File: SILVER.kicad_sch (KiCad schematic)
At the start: 51 parts, among them J1 Conn_01x13, J10 Conn_02x22_Odd_Even_MountingP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, J3 MPU6050, J4 MotorL, J5 MotorR, J6 XT60-M, J7 STLINK, J8 Conn_01x04_Pin, J9 Conn_02x22_Odd_Even_MountingP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, Q1 FCD600N60Z, Q2 FCD600N60Z, SW1 SW_DIP_x01, U1 VNH5019A-E, U2 VNH5019A-E, U4 LM2596S-5.0

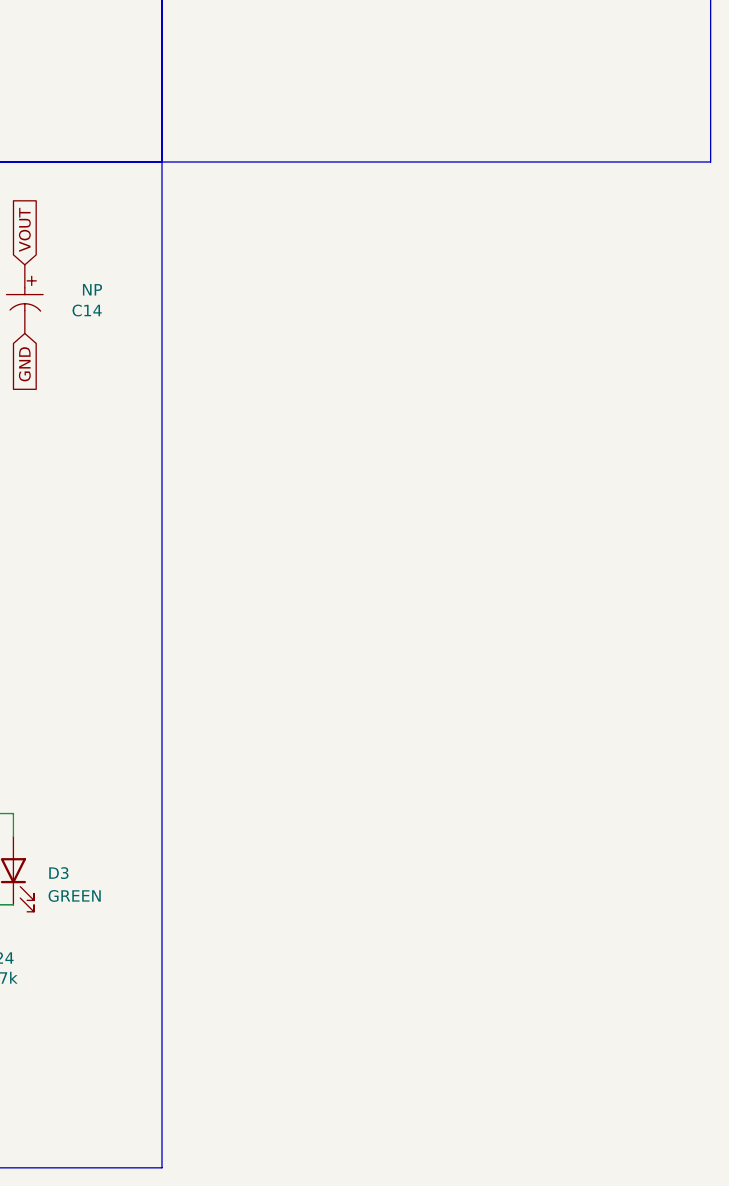
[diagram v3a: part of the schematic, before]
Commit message: Added ultrasonic sensor placement
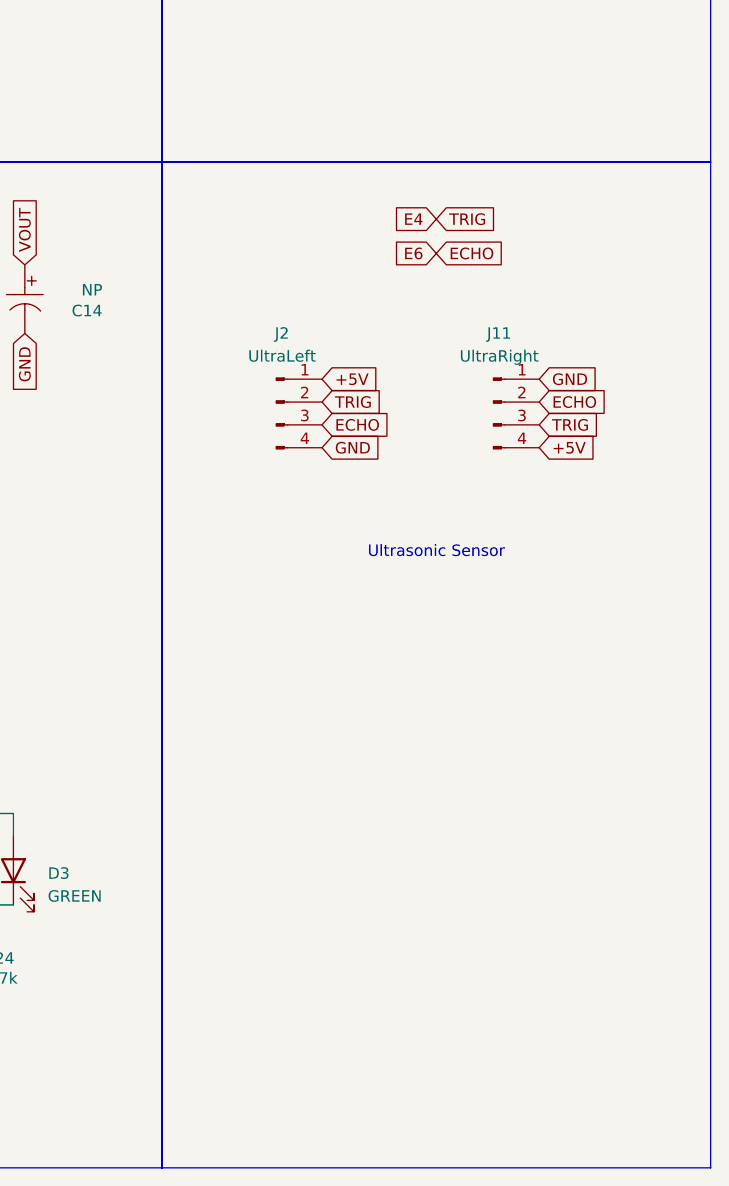
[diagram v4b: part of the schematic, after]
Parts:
- added J11: UltraRight, Connector_PinSocket_2.54mm:PinSocket_1x04_P2.54mm_Vertical, symbol Connector:Conn_01x04_Pin
- added J2: UltraLeft, Connector_PinSocket_2.54mm:PinSocket_1x04_P2.54mm_Vertical, symbol Connector:Conn_01x04_Pin
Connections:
- net +5V: now also J11.4 (Pin_4), J2.1 (Pin_1)
- net E4: now also J11.3 (Pin_3), J2.2 (Pin_2)
- net E6: now also J11.2 (Pin_2), J2.3 (Pin_3)
- net GND: now also J11.1 (Pin_1), J2.4 (Pin_4)
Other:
- note added: "Ultrasonic Sensor"

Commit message: pcbv1.0
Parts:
- removed C1, C5: 33nF, Capacitor_SMD:C_0805_2012Metric, symbol VNH5019-altium-import:root_3_33nF_
- removed C12, C15, C2, C4, C6, C8: 0.1u, Capacitor_SMD:C_0805_2012Metric, symbol VNH5019-altium-import:root_0_0.1u_
- removed C13, C14, C16, C17: NP, Capacitor_SMD:C_Elec_6.3x5.4, symbol VNH5019-altium-import:root_0_47uF_
- removed C18, C19: 330u, Capacitor_SMD:CP_Elec_8x10.5, symbol LM2596-altium-import:root_0_330u_
- removed C3, C7: 47uF, Capacitor_SMD:C_Elec_6.3x5.4, symbol VNH5019-altium-import:root_0_47uF_
- removed D3, D6: GREEN, LED_SMD:LED_0603_1608Metric, symbol Device:LED
- removed D4, D5: RED, LED_SMD:LED_0603_1608Metric, symbol Device:LED
- removed D7: SS34, Diode_SMD:D_SMA, symbol LM2596-altium-import:root_1_SS34_
- removed L2: 47uH, Inductor_SMD:L_12x12mm_H6mm, symbol LM2596-altium-import:root_0_47uH_
- removed Q1, Q2: FCD600N60Z, Package_TO_SOT_SMD:TO-252-2, symbol VNH5019-altium-import:root_1_FCD600N60Z_
- removed R1, R10: 10k, Resistor_SMD:R_0508_1220Metric, symbol VNH5019-altium-import:root_1_10k_
- removed R11, R12, R15, R2, R3, R6: 1k, Resistor_SMD:R_0508_1220Metric, symbol VNH5019-altium-import:root_0_1k_
- removed R16, R7: 1k, Resistor_SMD:R_0508_1220Metric, symbol VNH5019-altium-import:root_1_1k_
- removed R18, R9: 10k, Resistor_SMD:R_0508_1220Metric, symbol VNH5019-altium-import:root_0_10k_
- removed R24, R25: 4.7k, Resistor_SMD:R_0508_1220Metric, symbol VNH5019-altium-import:root_1_4.7k_
- removed U1, U2: VNH5019A-E, Package_SO:ST_MultiPowerSO-30, symbol VNH5019-altium-import:root_0_VNH5019A-E_
- removed U4: LM2596S-5.0, Package_TO_SOT_SMD:TO-263-5_TabPin3, symbol LM2596-altium-import:root_0_LM2596S-5.0_
- added D1: LED_RGBK, Connector_PinSocket_2.54mm:PinSocket_2x02_P2.54mm_Vertical, symbol Device:LED_RGBK
- added J12, J18: Conn_01x02_Pin, Connector_PinHeader_2.54mm:PinHeader_1x02_P2.54mm_Vertical, symbol Connector:Conn_01x02_Pin
- added J14, J15, J16, J17: Screw_Terminal_01x02, TerminalBlock:TerminalBlock_MaiXu_MX126-5.0-02P_1x02_P5.00mm, symbol Connector:Screw_Terminal_01x02
- J1: footprint Connector_FFC-FPC:Hirose_FH12-13S-0.5SH_1x13-1MP_P0.50mm_Horizontal -> Connector_PinHeader_2.54mm:PinHeader_1x13_P2.54mm_Vertical
- J7: now left out of the parts list
- SW1: footprint Library:SW_RB141C1100 -> Library:KCD11-101
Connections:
- net +12V: now also J14.1 (Pin_1)
- net +5V: now also J17.1 (Pin_1)
- net B8: now also J11.2 (Pin_2)
- net D12: now also J18.1 (Pin_1)
- net D13: now also J18.2 (Pin_2)
- net D14: now also J12.1 (Pin_1)
- net D15: now also J12.2 (Pin_2)
- net E6: no longer J11.2 (Pin_2)
- net E7: now also D1.1 (RA)
- net E8: now also D1.2 (GA)
- net E9: now also D1.3 (BA)
- net GND: now also D1.4 (K), J14.2 (Pin_2), J17.2 (Pin_2)
- net OUTA_L: now also J16.1 (Pin_1)
- net OUTA_R: now also J15.1 (Pin_1)
- net OUTB_L: now also J16.2 (Pin_2)
- net OUTB_R: now also J15.2 (Pin_2)
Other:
- note added: "Sensors connector"
- note removed: "35V"
- note removed: "Sensors ribbon flex connector"
- moved on the sheet: J1, J11, J2

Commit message: SILVER PCB v2.0
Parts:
- removed D1: LED_RGBK, Connector_PinSocket_2.54mm:PinSocket_2x02_P2.54mm_Vertical, symbol Device:LED_RGBK
- added D2: APFA3010, Connector_PinSocket_2.54mm:PinSocket_2x02_P2.54mm_Vertical, symbol LED:APFA3010
- added R1: R, Resistor_THT:R_Axial_DIN0204_L3.6mm_D1.6mm_P2.54mm_Vertical, symbol Device:R
- J1: footprint Connector_PinHeader_2.54mm:PinHeader_1x13_P2.54mm_Vertical -> Connector_PinHeader_2.54mm:PinHeader_1x13_P2.54mm_Vertical_SMD_Pin1Left
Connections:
- net +5V: now also R1.1
- net E7: now also D2.1 (R)
- net E8: now also D2.3 (G)
- net E9: now also D2.4 (B)
- new net: D2.2 (A), R1.2
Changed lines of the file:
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@@
 		)
 	)
-	(global_label "GND"
-		(shape input)
-		(at 209.55 214.63 180)
-		(fields_autoplaced yes)
-		(effects
-			(font
-				(size 1.27 1.27)
-			)
-			(justify right)
-		)
-		(property "Intersheetrefs" "${INTERSHEET_REFS}"
-			(at 202.6943 214.63 0)
-			(effects
-				(font
-					(size 1.27 1.27)
-				)
-				(justify right)
-				(hide yes)
-			)
-		)
-	)
 	(global_label "INT"
 		(shape input)
@@
 		)
 	)
+	(global_label "+5V"
+		(shape input)
+		(at 201.93 214.63 180)
+		(fields_autoplaced yes)
+		(effects
+			(font
+				(size 1.27 1.27)
+			)
+			(justify right)
+		)
+		(property "Intersheetrefs" "${INTERSHEET_REFS}"
+			(at 195.0743 214.63 0)
+			(effects
+				(font
+					(size 1.27 1.27)
+				)
+				(justify right)
+				(hide yes)
+			)
+		)
+	)
 	(global_label "E3"
 		(shape input)
@@
 	)
 	(symbol
+		(lib_id "Device:R")
+		(at 205.74 214.63 90)
+		(unit 1)
+		(exclude_from_sim no)
+		(in_bom yes)
+		(on_board yes)
+		(dnp no)
+		(fields_autoplaced yes)
+		(property "Reference" "R1"
+			(at 205.74 208.28 90)
+			(effects
+				(font
+					(size 1.27 1.27)
+				)
+			)
+		)
+		(property "Value" "R"
+			(at 205.74 210.82 90)
+			(effects
+				(font
+					(size 1.27 1.27)
+				)
+			)
+		)
+		(property "Footprint" "Resistor_THT:R_Axial_DIN0204_L3.6mm_D1.6mm_P2.54mm_Vertical"
+			(at 205.74 216.408 90)
+			(effects
+				(font
+					(size 1.27 1.27)
+				)
+				(hide yes)
+			)
+		)
+		(property "Datasheet" "~"
+			(at 205.74 214.63 0)
+			(effects
+				(font
+					(size 1.27 1.27)
+				)
+				(hide yes)
+			)
+		)
+		(property "Description" "Resistor"
+			(at 205.74 214.63 0)
+			(effects
+				(font
+					(size 1.27 1.27)
+				)
+				(hide yes)
+			)
+		)
+		(pin "1"
+		)
+		(pin "2"
+		)
+		(instances
+			(project ""
+				(path "/ac1a16b8-a2a7-4153-a4fd-a818d49ce2b8"
+					(reference "R1")
+					(unit 1)
+				)
+			)
+		)
+	)
+	(symbol
 		(lib_id "STLINK-altium-import:root_0_NUCLEO-F401-STLINKEXTRACT_")
 		(at 66.04 52.07 0)
@@
 			)
 		)
-		(property "Footprint" "Connector_PinHeader_2.54mm:PinHeader_1x13_P2.54mm_Vertical"
+		(property "Footprint" "Connector_PinHeader_2.54mm:PinHeader_1x13_P2.54mm_Vertical_SMD_Pin1Left"
 			(at 191.77 66.04 0)
 			(effects
@@
 	)
 	(symbol
-		(lib_id "Device:LED_RGBK")
-		(at 214.63 214.63 0)
-		(unit 1)
-		(exclude_from_sim no)
-		(in_bom yes)
-		(on_board yes)
-		(dnp no)
-		(fields_autoplaced yes)
-		(property "Reference" "D1"
-			(at 214.63 200.66 0)
-			(effects
-				(font
-					(size 1.27 1.27)
-				)
-			)
-		)
-		(property "Value" "LED_RGBK"
-			(at 214.63 203.2 0)
-			(effects
-				(font
-					(size 1.27 1.27)
-				)
-			)
-		)
-		(property "Footprint" "Connector_PinSocket_2.54mm:PinSocket_2x02_P2.54mm_Vertical"
-			(at 214.63 215.9 0)
-			(effects
-				(font
-					(size 1.27 1.27)
-				)
-				(hide yes)
-			)
-		)
-		(property "Datasheet" "~"
-			(at 214.63 215.9 0)
-			(effects
-				(font
-					(size 1.27 1.27)
-				)
-				(hide yes)
-			)
-		)
-		(property "Description" "RGB LED, red/green/blue/cathode"
-			(at 214.63 214.63 0)
-			(effects
-				(font
-					(size 1.27 1.27)
-				)
-				(hide yes)
-			)
-		)
-		(pin "2"
-		)
-		(pin "1"
-		)
-		(pin "4"
-		)
-		(pin "3"
-		)
-		(instances
-			(project ""
-				(path "/ac1a16b8-a2a7-4153-a4fd-a818d49ce2b8"
-					(reference "D1")
-					(unit 1)
-				)
-			)
-		)
-	)
-	(symbol
 		(lib_id "Switch:SW_DIP_x01")
 		(at 60.96 99.06 0)
@@
 					(unit 1)
 				)
+			)
+		)
+	)
+	(symbol
+		(lib_id "LED:APFA3010")
+		(at 214.63 214.63 0)
+		(mirror y)
+		(unit 1)
+		(exclude_from_sim no)
+		(in_bom yes)
+		(on_board yes)
+		(dnp no)
+		(property "Reference" "D2"
+			(at 214.63 200.66 0)
+			(effects
+				(font
+					(size 1.27 1.27)
+				)
+			)
+		)
+		(property "Value" "APFA3010"
+			(at 214.63 203.2 0)
+			(effects
+				(font
+					(size 1.27 1.27)
+				)
+			)
+		)
+		(property "Footprint" "Connector_PinSocket_2.54mm:PinSocket_2x02_P2.54mm_Vertical"
+			(at 214.63 201.93 0)
+			(effects
+				(font
+					(size 1.27 1.27)
+				)
+				(hide yes)
+			)
+		)
+		(property "Datasheet" "http://www.kingbrightusa.com/images/catalog/SPEC/APFA3010LSEEZGKQBKC.pdf"
+			(at 214.63 226.06 0)
+			(effects
+				(font
+					(size 1.27 1.27)
+				)
+				(hide yes)
+			)
+		)
+		(property "Description" "LED RGB, Common Anode, SMD, 3.0x1.5mm, Horizontal"
+			(at 214.63 214.63 0)
+			(effects
+				(font
+					(size 1.27 1.27)
+				)
+				(hide yes)
+			)
+		)
+		(pin "1"
+		)
+		(pin "2"
+		)
+		(pin "4"
+		)
+		(pin "3"
+		)
+		(instances
+			(project ""
+				(path "/ac1a16b8-a2a7-4153-a4fd-a818d49ce2b8"
+					(reference "D2")
+					(unit 1)
+				)
